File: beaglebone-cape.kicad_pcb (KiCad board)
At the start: 2 copper layers, 86.4 x 54.6 mm, 56 parts, among them P1 BEAGLEBONE_BLACK, P2 12V, P3 RED_LIGHT, P4 JUMPERS, P5 GREEN_LIGHT, P6 CONN_01X05, P7 NC/NO JUMPER, P8 NC/NO JUMPER, P9 DOOR STRIKE/MAGNET, Q1 2N7000, Q2 2N7000, Q3 2N7000, Q4 2N7000, SW1 PWR_SWITCH, SW2 RESET_SWITCH, U1 24C256, U2 V7805-2000, U3 4N25, U4 4N25

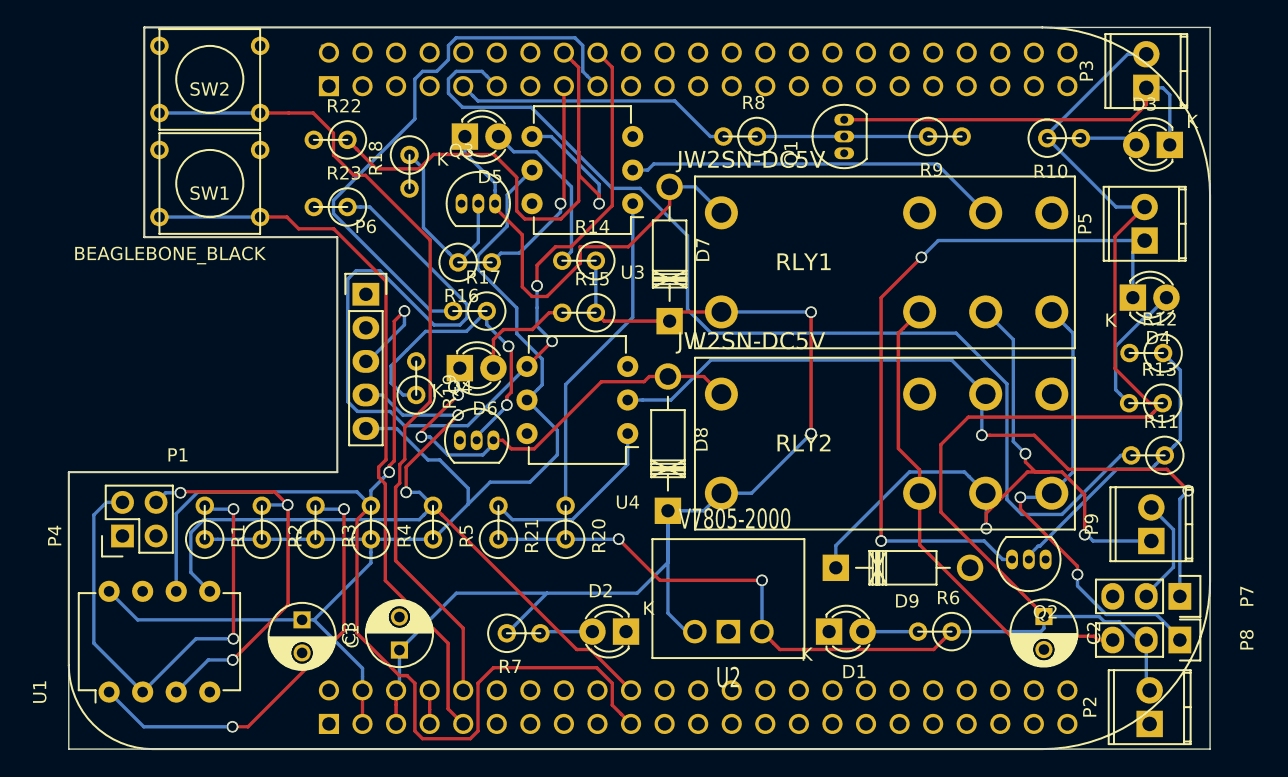
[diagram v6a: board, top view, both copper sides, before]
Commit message: only 2 GND nets to connect.  Not sure what's wrong w/ them
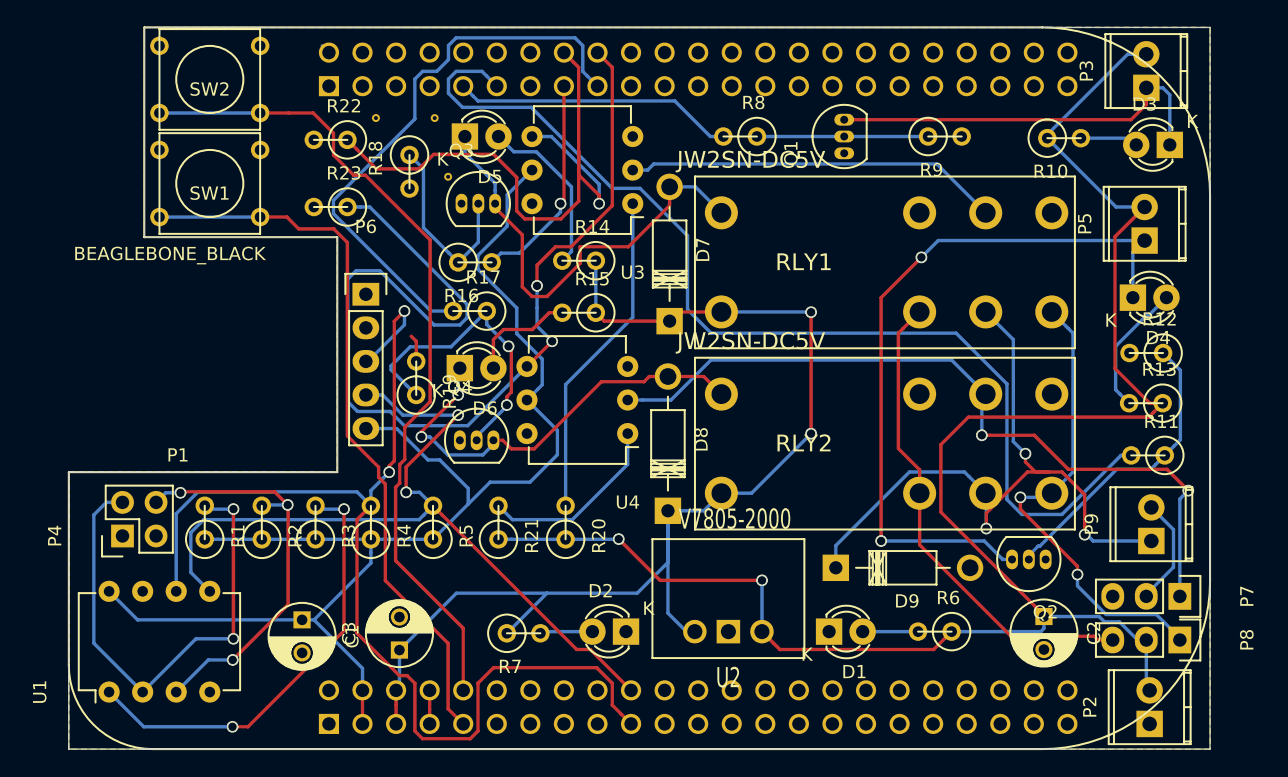
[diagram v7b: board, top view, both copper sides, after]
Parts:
- added REF**: VIA-0.6mm, beagleboard.new:VIA-0.6mm, F.Cu at (123.2, 98.2)
- added REF**: VIA-0.6mm, beagleboard.new:VIA-0.6mm, F.Cu at (122.2, 93.7)
- added REF**: VIA-0.6mm, beagleboard.new:VIA-0.6mm, F.Cu at (117.7, 93.7)
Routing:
- net GND: track 0.72 -> 2.78 mm
- net Net-(Q4-Pad2): track 24.2 -> 23.6 mm
- added copper zone on B.Cu, net GND
- added copper zone on F.Cu, net GND
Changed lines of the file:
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@@
 (kicad_pcb (version 4) (host pcbnew 4.0.1-2.201512121406+6195~38~ubuntu15.10.1-stable)
   (general
-    (links 128)
-    (no_connects 38)
+    (links 133)
+    (no_connects 2)
     (area 94.437999 85.039999 180.898001 139.750001)
     (thickness 1.6)
     (drawings 8)
-    (tracks 521)
+    (tracks 522)
     (zones 0)
-    (modules 56)
+    (modules 59)
     (nets 115)
   )
@@
   )
   (layers
-    (0 Top mixed)
+    (0 Top mixed hide)
     (31 Bottom mixed)
     (32 B.Adhes user)
@@
     (uvia_drill 0.127)
   )
+  (module beagleboard.new:VIA-0.6mm (layer Top)
+    (at 123.19 98.171)
+    (fp_text reference REF** (at 0 -0.508) (layer F.SilkS) hide
+      (effects (font (size 1 1) (thickness 0.15)))
+    )
+    (fp_text value VIA-0.6mm (at 0 -3.048) (layer F.Fab) hide
+      (effects (font (size 1 1) (thickness 0.15)))
+    )
+    (pad 1 thru_hole circle (at 0 -1.778) (size 0.6 0.6) (drill 0.3) (layers *.Cu)
+      (net 7 GND) (zone_connect 2))
+  )
+  (module beagleboard.new:VIA-0.6mm (layer Top)
+    (at 122.174 93.726)
+    (fp_text reference REF** (at 0 -0.508) (layer F.SilkS) hide
+      (effects (font (size 1 1) (thickness 0.15)))
+    )
+    (fp_text value VIA-0.6mm (at 0 -3.048) (layer F.Fab) hide
+      (effects (font (size 1 1) (thickness 0.15)))
+    )
+    (pad 1 thru_hole circle (at 0 -1.778) (size 0.6 0.6) (drill 0.3) (layers *.Cu)
+      (net 7 GND) (zone_connect 2))
+  )
   (module Discret:R1 (layer Top)
     (at 117.348 122.555 90)
@@
       (rotate (xyz 0 0 0))
     )
+  )
+  (module beagleboard.new:VIA-0.6mm (layer Top)
+    (at 117.729 93.726)
+    (fp_text reference REF** (at 0 -0.508) (layer F.SilkS) hide
+      (effects (font (size 1 1) (thickness 0.15)))
+    )
+    (fp_text value VIA-0.6mm (at 0 -3.048) (layer F.Fab) hide
+      (effects (font (size 1 1) (thickness 0.15)))
+    )
+    (pad 1 thru_hole circle (at 0 -1.778) (size 0.6 0.6) (drill 0.3) (layers *.Cu)
+      (net 7 GND) (zone_connect 2))
   )
   (gr_line (start 94.488 139.7) (end 94.488 118.745) (angle 90) (layer Edge.Cuts) (width 0.1))
@@
   (segment (start 121.793 137.795) (end 121.793 136.71737) (width 0.254) (layer Top) (net 6))
   (segment (start 121.793 136.71737) (end 121.793 135.255) (width 0.254) (layer Top) (net 6))
+  (segment (start 120.777 110.363) (end 120.777 108.839) (width 0.254) (layer Top) (net 7))
+  (segment (start 120.777 108.839) (end 120.396 108.458) (width 0.254) (layer Top) (net 7))
   (segment (start 113.665 86.487) (end 114.173 86.995) (width 0.254) (layer Bottom) (net 7))
   (segment (start 128.384399 106.322469) (end 128.384399 108.259109) (width 0.254) (layer Bottom) (net 8))
@@
   (segment (start 116.557828 98.679) (end 115.57 98.679) (width 0.254) (layer Bottom) (net 37))
   (segment (start 115.59539 104.134928) (end 115.666519 104.063799) (width 0.254) (layer Bottom) (net 37))
+  (segment (start 124.333 137.795) (end 123.19 136.652) (width 0.254) (layer Top) (net 66))
+  (segment (start 117.932167 119.12905) (end 117.932167 118.36095) (width 0.254) (layer Top) (net 66))
+  (segment (start 123.19 136.652) (end 123.19 131.699) (width 0.254) (layer Top) (net 66))
+  (segment (start 115.57 101.366318) (end 114.533682 100.33) (width 0.254) (layer Top) (net 66))
+  (segment (start 123.19 131.699) (end 118.440167 126.949167) (width 0.254) (layer Top) (net 66))
+  (segment (start 114.533682 100.33) (end 111.887 100.33) (width 0.254) (layer Top) (net 66))
+  (segment (start 118.440167 126.949167) (end 118.440167 119.63705) (width 0.254) (layer Top) (net 66))
+  (segment (start 117.932167 118.36095) (end 115.57 115.998783) (width 0.254) (layer Top) (net 66))
+  (segment (start 111.887 100.33) (end 110.998 99.441) (width 0.254) (layer Top) (net 66))
+  (segment (start 118.440167 119.63705) (end 117.932167 119.12905) (width 0.254) (layer Top) (net 66))
+  (segment (start 115.57 115.998783) (end 115.57 101.366318) (width 0.254) (layer Top) (net 66))
   (segment (start 110.998 99.441) (end 108.966 99.441) (width 0.254) (layer Top) (net 66))
-  (segment (start 124.333 137.795) (end 123.19 136.652) (width 0.254) (layer Top) (net 66))
-  (segment (start 123.19 136.652) (end 123.19 131.699) (width 0.254) (layer Top) (net 66))
-  (segment (start 123.19 131.699) (end 118.440167 126.949167) (width 0.254) (layer Top) (net 66))
-  (segment (start 118.440167 126.949167) (end 118.440167 119.63705) (width 0.254) (layer Top) (net 66))
-  (segment (start 118.440167 119.63705) (end 117.932167 119.12905) (width 0.254) (layer Top) (net 66))
-  (segment (start 117.932167 119.12905) (end 117.932167 118.36095) (width 0.254) (layer Top) (net 66))
-  (segment (start 117.932167 118.36095) (end 118.491 117.802117) (width 0.254) (layer Top) (net 66))
-  (segment (start 118.491 117.802117) (end 118.491 104.287318) (width 0.254) (layer Top) (net 66))
-  (segment (start 118.491 104.287318) (end 114.533682 100.33) (width 0.254) (layer Top) (net 66))
-  (segment (start 114.533682 100.33) (end 111.887 100.33) (width 0.254) (layer Top) (net 66))
-  (segment (start 111.887 100.33) (end 110.998 99.441) (width 0.254) (layer Top) (net 66))
   (segment (start 108.966 99.441) (end 101.346 99.441) (width 0.254) (layer Bottom) (net 66))
   (segment (start 111.125 91.567) (end 108.966 91.567) (width 0.254) (layer Top) (net 67))
@@
   (segment (start 125.476 98.425) (end 125.476 101.346) (width 0.254) (layer Bottom) (net 105))
   (segment (start 125.476 101.346) (end 123.952 102.87) (width 0.254) (layer Bottom) (net 105))
-  (segment (start 121.490218 108.089712) (end 120.10593 109.474) (width 0.254) (layer Bottom) (net 106))
-  (segment (start 120.10593 109.474) (end 118.872 110.70793) (width 0.254) (layer Bottom) (net 106))
+  (segment (start 120.078501 112.204501) (end 120.777 112.903) (width 0.254) (layer Bottom) (net 106))
+  (segment (start 118.872 110.998) (end 120.078501 112.204501) (width 0.254) (layer Bottom) (net 106))
+  (segment (start 118.872 110.70793) (end 118.872 110.998) (width 0.254) (layer Bottom) (net 106))
+  (segment (start 120.321829 109.258101) (end 118.872 110.70793) (width 0.254) (layer Bottom) (net 106))
+  (segment (start 123.405899 109.258101) (end 120.321829 109.258101) (width 0.254) (layer Bottom) (net 106))
+  (segment (start 126.111 106.553) (end 123.405899 109.258101) (width 0.254) (layer Bottom) (net 106))
   (segment (start 127.762 109.22) (end 126.111 107.569) (width 0.254) (layer Bottom) (net 106))
   (segment (start 126.111 107.569) (end 126.111 106.553) (width 0.254) (layer Bottom) (net 106))
@@
   (segment (start 127.635 113.74501) (end 127.635 113.665) (width 0.254) (layer Bottom) (net 106))
   (via (at 127.635 113.665) (size 0.889) (drill 0.635) (layers Top Bottom) (net 106))
-  (segment (start 120.777 112.903) (end 119.789172 112.903) (width 0.254) (layer Bottom) (net 106))
-  (segment (start 119.789172 112.903) (end 118.872 111.985828) (width 0.254) (layer Bottom) (net 106))
-  (segment (start 118.872 111.985828) (end 118.872 110.70793) (width 0.254) (layer Bottom) (net 106))
-  (segment (start 126.111 106.553) (end 124.574288 108.089712) (width 0.254) (layer Bottom) (net 106))
-  (segment (start 124.574288 108.089712) (end 121.490218 108.089712) (width 0.254) (layer Bottom) (net 106))
   (segment (start 132.08 112.1156) (end 137.16 107.0356) (width 0.254) (layer Bottom) (net 107))
   (segment (start 137.16 107.0356) (end 137.16 98.425) (width 0.254) (layer Bottom) (net 107))
@@
   (segment (start 163.869 99.12) (end 160.16919 95.42019) (width 0.254) (layer Bottom) (net 109))
   (segment (start 160.16919 95.42019) (end 138.75618 95.42019) (width 0.254) (layer Bottom) (net 109))
+  (zone (net 7) (net_name GND) (layer Top) (hatch edge 0.508)
+    (connect_pads (clearance 0.508))
+    (min_thickness 0.254)
+    (fill yes (arc_segments 16) (thermal_gap 0.508) (thermal_bridge_width 0.508))
+    (polygon
+      (pts
+        (xy 180.848 139.7) (xy 94.488 139.7) (xy 94.488 118.745) (xy 114.808 118.745) (xy 114.808 100.965)
+        (xy 100.203 100.965) (xy 100.203 85.09) (xy 180.848 85.09) (xy 180.848 139.7)
+      )
+    )
+  )
+  (zone (net 7) (net_name GND) (layer Bottom) (hatch edge 0.508)
+    (connect_pads (clearance 0.508))
+    (min_thickness 0.254)
+    (fill yes (arc_segments 16) (thermal_gap 0.508) (thermal_bridge_width 0.508))
+    (polygon
+      (pts
+        (xy 180.848 139.7) (xy 94.488 139.7) (xy 94.488 118.745) (xy 114.808 118.745) (xy 114.808 100.965)
+        (xy 100.203 100.965) (xy 100.203 85.09) (xy 180.848 85.09) (xy 180.848 139.7)
+      )
+    )
+  )
 )
